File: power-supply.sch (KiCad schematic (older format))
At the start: 0 parts

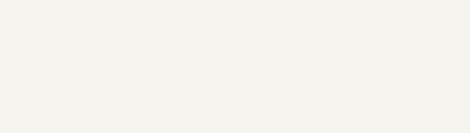
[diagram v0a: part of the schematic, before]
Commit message: Changed the controller symbol for the LPC11C24 added some of the support components,played with the larger blocks
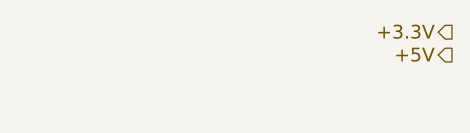
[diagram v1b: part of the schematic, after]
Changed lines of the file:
@@
-EESchema Schematic File Version 2  date 4/14/2013 3:01:00 AM
+EESchema Schematic File Version 2  date 4/14/2013 3:47:51 AM
 LIBS:power
 LIBS:device
@@
 $Descr A4 11693 8268
 encoding utf-8
-Sheet 4 6
+Sheet 6 6
 Title ""
 Date "14 apr 2013"
@@
 Text HLabel 2350 3400 0    60   UnSpc ~ 0
 GND
+Text HLabel 8950 3100 0    60   Output ~ 0
++3.3V
+Text HLabel 8950 3200 0    60   Output ~ 0
++5V
 $EndSCHEMATC

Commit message: changed the voltage lbaels to global labels
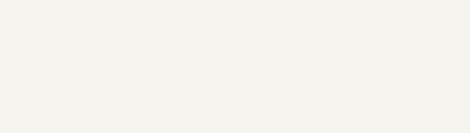
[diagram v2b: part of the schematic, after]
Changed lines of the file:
@@
-EESchema Schematic File Version 2  date 4/14/2013 3:47:51 AM
+EESchema Schematic File Version 2  date 4/14/2013 1:14:12 PM
 LIBS:power
 LIBS:device
@@
 $Descr A4 11693 8268
 encoding utf-8
-Sheet 6 6
+Sheet 6 7
 Title ""
 Date "14 apr 2013"
@@
 Text HLabel 2350 3400 0    60   UnSpc ~ 0
 GND
-Text HLabel 8950 3100 0    60   Output ~ 0
-+3.3V
-Text HLabel 8950 3200 0    60   Output ~ 0
-+5V
 $EndSCHEMATC

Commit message: did the power sheet
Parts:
- added C?: 10uF, ~, symbol C
- added C? (x2): 100nF, ~, symbol C
- added C?: 3.3nF, ~, symbol C
- added C?: C, ~, symbol C
- added C?: 22uF, ~, symbol C
- added C?: 22nF, ~, symbol C
- added L?: 15uH, ~, symbol INDUCTOR
- added R?: 62k, ~, symbol R
- added R?: 11.8k, ~, symbol R
- added R?: 20k, ~, symbol R
- added R?: 20, ~, symbol R
- added U?: RT7247AHGSP, symbol RT7247AHGSP
- added U?: LM137H, TO-39, symbol LM137H
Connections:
- net labels added: +3.3V, +5V
- wire segments 0 -> 41

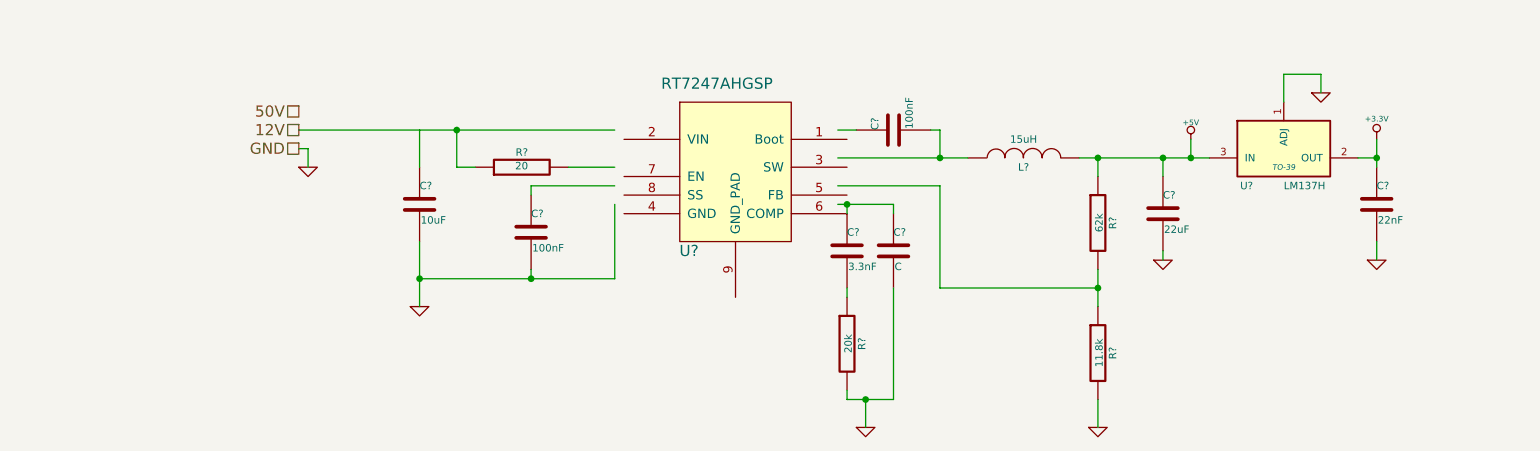
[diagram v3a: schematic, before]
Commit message: updated the power circut to include the more hidden preferences on the data sheet
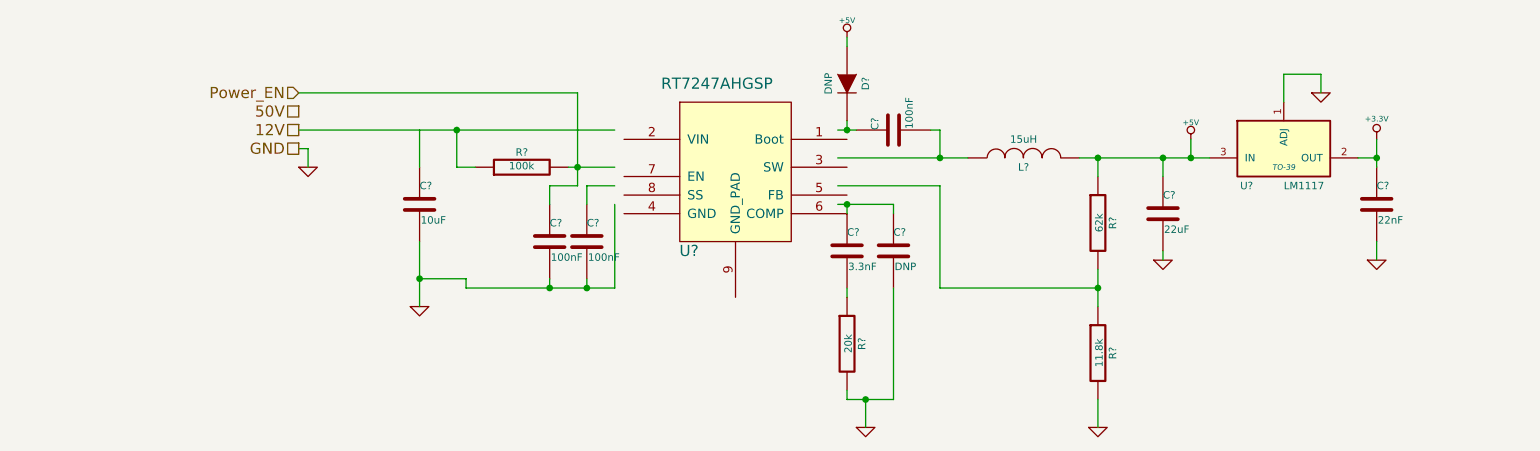
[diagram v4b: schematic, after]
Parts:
- added C?: 100nF, ~, symbol C
- added D?: DNP, ~, symbol DIODE
- C?: value C -> DNP
- R?: value 20 -> 100k
- U?: value LM137H -> LM1117
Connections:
- net labels added: Power_EN
- wire segments 41 -> 65
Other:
- moved on the sheet: C?
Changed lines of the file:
@@
-EESchema Schematic File Version 2  date 4/15/2013 12:24:14 AM
+EESchema Schematic File Version 2  date 4/15/2013 12:46:04 AM
 LIBS:power
 LIBS:device
@@
 L C C?
 U 1 1 516B7AF4
-P 3600 3700
-F 0 "C?" H 3600 3800 40  0000 L CNN
-F 1 "100nF" H 3606 3615 40  0000 L CNN
-F 2 "~" H 3638 3550 30  0000 C CNN
-F 3 "~" H 3600 3700 60  0000 C CNN
-	1    3600 3700
+P 3900 3750
+F 0 "C?" H 3900 3850 40  0000 L CNN
+F 1 "100nF" H 3906 3665 40  0000 L CNN
+F 2 "~" H 3938 3600 30  0000 C CNN
+F 3 "~" H 3900 3750 60  0000 C CNN
+	1    3900 3750
 	1    0    0    -1
 $EndComp
@@
 P 5550 3800
 F 0 "C?" H 5550 3900 40  0000 L CNN
-F 1 "C" H 5556 3715 40  0000 L CNN
+F 1 "DNP" H 5556 3715 40  0000 L CNN
 F 2 "~" H 5588 3650 30  0000 C CNN
 F 3 "~" H 5550 3800 60  0000 C CNN
@@
 $EndComp
 Wire Wire Line
-	2350 3150 4050 3150
-Wire Wire Line
-	3000 3750 3000 4100
+	2350 3150 3200 3150
+Wire Wire Line
+	3200 3150 4050 3150
+Wire Wire Line
+	3000 3750 3000 3950
+Wire Wire Line
+	3000 3950 3000 4100
 Wire Wire Line
 	3000 3350 3000 3150
 Wire Wire Line
-	3600 3500 3600 3450
-Wire Wire Line
-	3600 3450 4050 3450
-Wire Wire Line
-	4050 3950 4050 3550
-Wire Wire Line
-	3000 3950 4050 3950
-Wire Wire Line
-	3600 3950 3600 3900
+	3900 3550 3900 3450
+Wire Wire Line
+	3900 3450 4050 3450
+Wire Wire Line
+	4050 4000 4050 3550
+Wire Wire Line
+	3000 3950 3250 3950
+Wire Wire Line
+	3250 4000 3700 4000
+Wire Wire Line
+	3700 4000 3900 4000
+Wire Wire Line
+	3900 4000 4050 4000
+Wire Wire Line
+	3900 4000 3900 3950
 Connection ~ 3000 3950
-Connection ~ 3600 3950
 Wire Wire Line
 	5300 3600 5300 3550
 Wire Wire Line
-	5250 3550 5550 3550
+	5250 3550 5300 3550
+Wire Wire Line
+	5300 3550 5550 3550
 Wire Wire Line
 	5550 3550 5550 3600
@@
 	5550 4600 5550 4000
 Wire Wire Line
-	5300 4600 5550 4600
+	5300 4600 5400 4600
+Wire Wire Line
+	5400 4600 5550 4600
 Wire Wire Line
 	5300 4600 5300 4550
@@
 	5300 4050 5300 4000
 Wire Wire Line
-	5250 3300 5950 3300
+	5250 3300 5800 3300
+Wire Wire Line
+	5800 3300 5950 3300
 Wire Wire Line
 	5250 3450 5800 3450
@@
 	5800 4000 6650 4000
 Wire Wire Line
-	6650 3900 6650 4100
+	6650 3900 6650 4000
+Wire Wire Line
+	6650 4000 6650 4100
 Connection ~ 6650 4000
 Wire Wire Line
 	6650 3400 6650 3300
 Wire Wire Line
-	6550 3300 7250 3300
+	6550 3300 6650 3300
+Wire Wire Line
+	6650 3300 7000 3300
+Wire Wire Line
+	7000 3300 7150 3300
+Wire Wire Line
+	7150 3300 7250 3300
 Wire Wire Line
 	5800 3450 5800 4000
 Wire Wire Line
-	5250 3150 5350 3150
+	5250 3150 5300 3150
+Wire Wire Line
+	5300 3150 5350 3150
 Wire Wire Line
 	5800 3150 5750 3150
@@
 P 7650 3250
 F 0 "U?" H 7450 3050 40  0000 C CNN
-F 1 "LM137H" H 7650 3050 40  0000 L CNN
+F 1 "LM1117" H 7650 3050 40  0000 L CNN
 F 2 "TO-39" H 7650 3150 30  0000 C CIN
 F 3 "~" H 7650 3250 60  0000 C CNN
@@
 	8050 3300 8150 3300
 Wire Wire Line
-	8150 3200 8150 3350
+	8150 3200 8150 3300
+Wire Wire Line
+	8150 3300 8150 3350
 $Comp
 L C C?
@@
 P 3550 3350
 F 0 "R?" V 3630 3350 40  0000 C CNN
-F 1 "20" V 3557 3351 40  0000 C CNN
+F 1 "100k" V 3557 3351 40  0000 C CNN
 F 2 "~" V 3480 3350 30  0000 C CNN
 F 3 "~" H 3550 3350 30  0000 C CNN
@@
 Connection ~ 3200 3150
 Wire Wire Line
-	3800 3350 4050 3350
+	3800 3350 3850 3350
+Wire Wire Line
+	3850 3350 4050 3350
 $Comp
 L GND #PWR?
@@
 Wire Wire Line
 	2400 3250 2350 3250
+$Comp
+L DIODE D?
+U 1 1 516B8761
+P 5300 2900
+F 0 "D?" H 5300 3000 40  0000 C CNN
+F 1 "DNP" H 5300 2800 40  0000 C CNN
+F 2 "~" H 5300 2900 60  0000 C CNN
+F 3 "~" H 5300 2900 60  0000 C CNN
+	1    5300 2900
+	0    1    1    0
+$EndComp
+Wire Wire Line
+	5300 3100 5300 3150
+Connection ~ 5300 3150
+$Comp
+L +5V #PWR?
+U 1 1 516B87A2
+P 5300 2650
+F 0 "#PWR?" H 5300 2740 20  0001 C CNN
+F 1 "+5V" H 5300 2740 30  0000 C CNN
+F 2 "" H 5300 2650 60  0000 C CNN
+F 3 "" H 5300 2650 60  0000 C CNN
+	1    5300 2650
+	1    0    0    -1
+$EndComp
+Wire Wire Line
+	5300 2700 5300 2650
+$Comp
+L C C?
+U 1 1 516B8BF3
+P 3700 3750
+F 0 "C?" H 3700 3850 40  0000 L CNN
+F 1 "100nF" H 3706 3665 40  0000 L CNN
+F 2 "~" H 3738 3600 30  0000 C CNN
+F 3 "~" H 3700 3750 60  0000 C CNN
+	1    3700 3750
+	1    0    0    -1
+$EndComp
+Wire Wire Line
+	3250 3950 3250 4000
+Connection ~ 3900 4000
+Wire Wire Line
+	3700 3950 3700 4000
+Connection ~ 3700 4000
+Wire Wire Line
+	3700 3550 3700 3450
+Wire Wire Line
+	3850 3450 3700 3450
+Wire Wire Line
+	3850 2950 3850 3350
+Wire Wire Line
+	3850 3350 3850 3450
+Connection ~ 3850 3350
+Text HLabel 2350 2950 0    60   Input ~ 0
+Power_EN
+Wire Wire Line
+	2350 2950 3850 2950
 $EndSCHEMATC

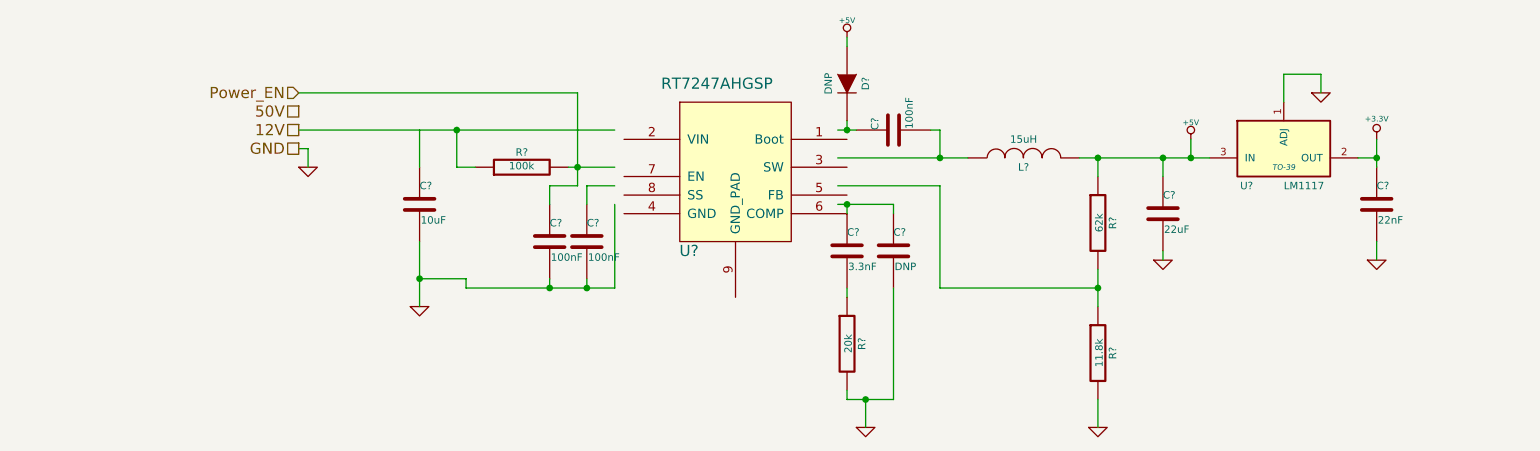
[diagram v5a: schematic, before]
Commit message: power updated still need to add underpad also changed input connector to 5 pin and added fuses, added current sense with op-amp for solinoids
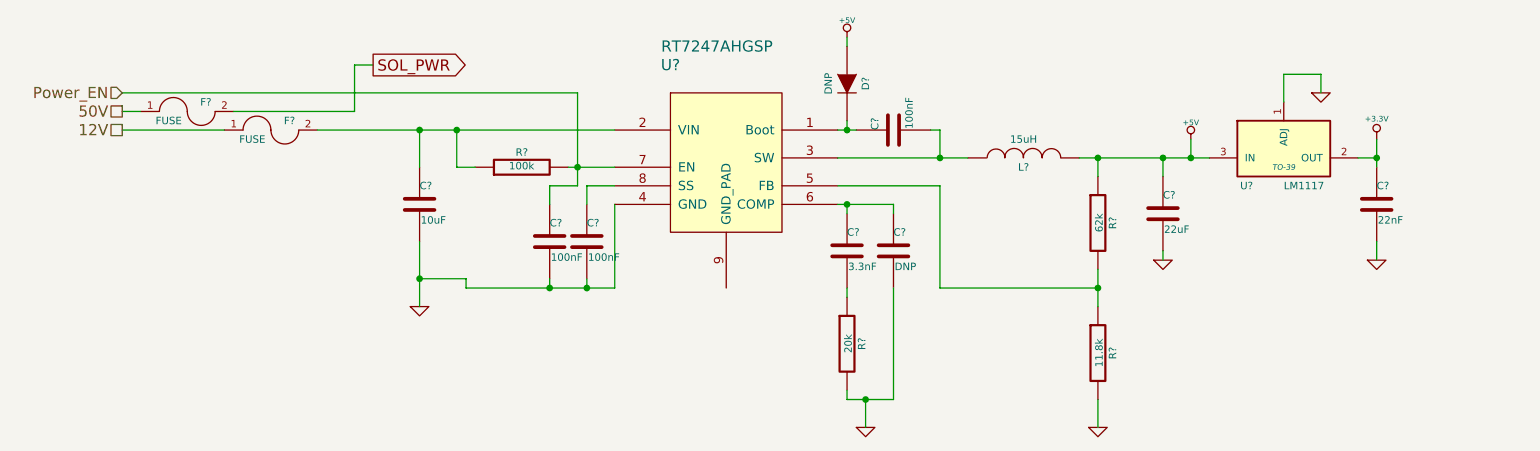
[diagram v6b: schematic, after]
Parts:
- removed U?: RT7247AHGSP, symbol RT7247AHGSP
- added F? (x2): FUSE, ~, symbol FUSE
- added U?: RT7247AHGSP, symbol RT7247AHGSP
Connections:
- net labels added: SOL_PWR
- wire segments 65 -> 53
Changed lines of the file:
@@
-EESchema Schematic File Version 2  date 4/15/2013 1:22:57 AM
+EESchema Schematic File Version 2  date 4/16/2013 12:48:50 AM
 LIBS:power
 LIBS:device
@@
 LIBS:pinball_components
 LIBS:micro-controller
+LIBS:CurrentSense
+LIBS:pinball-power
 LIBS:base-module-cache
 EELAYER 27 0
@@
 $Descr A4 11693 8268
 encoding utf-8
-Sheet 7 7
+Sheet 6 8
 Title ""
-Date "15 apr 2013"
+Date "16 apr 2013"
 Rev ""
 Comp ""
@@
 Comment4 ""
 $EndDescr
-Text HLabel 2350 3050 0    60   UnSpc ~ 0
+Text HLabel 1400 3050 0    60   UnSpc ~ 0
 50V
-Text HLabel 2350 3150 0    60   UnSpc ~ 0
+Text HLabel 1400 3150 0    60   UnSpc ~ 0
 12V
-Text HLabel 2350 3250 0    60   UnSpc ~ 0
-GND
-$Comp
-L RT7247AHGSP U?
-U 1 1 516B7ABB
-P 4650 3400
-F 0 "U?" H 4450 3000 60  0000 C CNN
-F 1 "RT7247AHGSP" H 4600 3900 60  0000 C CNN
-F 2 "" H 4650 3400 60  0000 C CNN
-F 3 "" H 4650 3400 60  0000 C CNN
-	1    4650 3400
-	1    0    0    -1
-$EndComp
 $Comp
 L C C?
@@
 	1    0    0    -1
 $EndComp
-Wire Wire Line
-	2350 3150 3200 3150
-Wire Wire Line
-	3200 3150 4050 3150
-Wire Wire Line
-	3000 3750 3000 3950
-Wire Wire Line
-	3000 3950 3000 4100
-Wire Wire Line
-	3000 3350 3000 3150
-Wire Wire Line
-	3900 3550 3900 3450
-Wire Wire Line
-	3900 3450 4050 3450
-Wire Wire Line
-	4050 4000 4050 3550
-Wire Wire Line
-	3000 3950 3250 3950
-Wire Wire Line
-	3250 4000 3700 4000
-Wire Wire Line
-	3700 4000 3900 4000
-Wire Wire Line
-	3900 4000 4050 4000
-Wire Wire Line
-	3900 4000 3900 3950
-Connection ~ 3000 3950
-Wire Wire Line
-	5300 3600 5300 3550
-Wire Wire Line
-	5250 3550 5300 3550
-Wire Wire Line
-	5300 3550 5550 3550
-Wire Wire Line
-	5550 3550 5550 3600
-Connection ~ 5300 3550
-Wire Wire Line
-	5550 4600 5550 4000
-Wire Wire Line
-	5300 4600 5400 4600
-Wire Wire Line
-	5400 4600 5550 4600
-Wire Wire Line
-	5300 4600 5300 4550
-Wire Wire Line
-	5300 4050 5300 4000
-Wire Wire Line
-	5250 3300 5800 3300
-Wire Wire Line
-	5800 3300 5950 3300
-Wire Wire Line
-	5250 3450 5800 3450
-Wire Wire Line
-	5800 4000 6650 4000
-Wire Wire Line
-	6650 3900 6650 4000
-Wire Wire Line
-	6650 4000 6650 4100
-Connection ~ 6650 4000
-Wire Wire Line
-	6650 3400 6650 3300
-Wire Wire Line
-	6550 3300 6650 3300
-Wire Wire Line
-	6650 3300 7000 3300
-Wire Wire Line
-	7000 3300 7150 3300
-Wire Wire Line
-	7150 3300 7250 3300
-Wire Wire Line
-	5800 3450 5800 4000
-Wire Wire Line
-	5250 3150 5300 3150
-Wire Wire Line
-	5300 3150 5350 3150
-Wire Wire Line
-	5800 3150 5750 3150
-Wire Wire Line
-	5800 3300 5800 3150
-Connection ~ 5800 3300
-Wire Wire Line
-	6650 4750 6650 4600
-Wire Wire Line
-	5400 4750 5400 4600
-Connection ~ 5400 4600
-Connection ~ 6650 3300
 $Comp
 L GND #PWR?
@@
 	1    0    0    -1
 $EndComp
-Wire Wire Line
-	7000 3850 7000 3800
 $Comp
 L +5V #PWR?
@@
 	1    0    0    -1
 $EndComp
-Wire Wire Line
-	7150 3300 7150 3200
-Wire Wire Line
-	7000 3400 7000 3300
-Connection ~ 7000 3300
 $Comp
 L LM137H U?
@@
 	1    0    0    -1
 $EndComp
-Connection ~ 7150 3300
 $Comp
 L GND #PWR?
@@
 	1    0    0    -1
 $EndComp
-Wire Wire Line
-	7850 2950 7850 2850
-Wire Wire Line
-	7850 2850 7650 2850
-Wire Wire Line
-	7650 2850 7650 3000
 $Comp
 L +3.3V #PWR?
@@
 	1    0    0    -1
 $EndComp
-Wire Wire Line
-	8050 3300 8150 3300
-Wire Wire Line
-	8150 3200 8150 3300
-Wire Wire Line
-	8150 3300 8150 3350
 $Comp
 L C C?
@@
 	1    0    0    -1
 $EndComp
-Wire Wire Line
-	8150 3850 8150 3750
-Connection ~ 8150 3300
 $Comp
 L R R?
@@
 	0    -1   -1   0
 $EndComp
-Wire Wire Line
-	3300 3350 3200 3350
-Wire Wire Line
-	3200 3350 3200 3150
-Connection ~ 3200 3150
-Wire Wire Line
-	3800 3350 3850 3350
-Wire Wire Line
-	3850 3350 4050 3350
-$Comp
-L GND #PWR?
-U 1 1 516B82F2
-P 2400 3350
-F 0 "#PWR?" H 2400 3350 30  0001 C CNN
-F 1 "GND" H 2400 3280 30  0001 C CNN
-F 2 "" H 2400 3350 60  0000 C CNN
-F 3 "" H 2400 3350 60  0000 C CNN
-	1    2400 3350
-	1    0    0    -1
-$EndComp
-Wire Wire Line
-	2400 3350 2400 3250
-Wire Wire Line
-	2400 3250 2350 3250
 $Comp
 L DIODE D?
@@
 	0    1    1    0
 $EndComp
-Wire Wire Line
-	5300 3100 5300 3150
-Connection ~ 5300 3150
 $Comp
 L +5V #PWR?
@@
 	1    0    0    -1
 $EndComp
-Wire Wire Line
-	5300 2700 5300 2650
 $Comp
 L C C?
@@
 	1    0    0    -1
 $EndComp
+Text HLabel 1400 2950 0    60   Input ~ 0
+Power_EN
+Wire Wire Line
+	3000 3750 3000 4100
+Wire Wire Line
+	3000 3350 3000 3150
+Wire Wire Line
+	3900 3550 3900 3450
+Wire Wire Line
+	3900 3450 4050 3450
+Wire Wire Line
+	4050 4000 4050 3550
+Wire Wire Line
+	3000 3950 3250 3950
+Wire Wire Line
+	3250 4000 4050 4000
+Wire Wire Line
+	3900 4000 3900 3950
+Connection ~ 3000 3950
+Wire Wire Line
+	5300 3600 5300 3550
+Wire Wire Line
+	5250 3550 5550 3550
+Wire Wire Line
+	5550 3550 5550 3600
+Connection ~ 5300 3550
+Wire Wire Line
+	5550 4600 5550 4000
+Wire Wire Line
+	5300 4600 5550 4600
+Wire Wire Line
+	5300 4600 5300 4550
+Wire Wire Line
+	5300 4050 5300 4000
+Wire Wire Line
+	5250 3300 5950 3300
+Wire Wire Line
+	5250 3450 5800 3450
+Wire Wire Line
+	5800 4000 6650 4000
+Wire Wire Line
+	6650 3900 6650 4100
+Connection ~ 6650 4000
+Wire Wire Line
+	6650 3400 6650 3300
+Wire Wire Line
+	6550 3300 7250 3300
+Wire Wire Line
+	5800 3450 5800 4000
+Wire Wire Line
+	5250 3150 5350 3150
+Wire Wire Line
+	5800 3150 5750 3150
+Wire Wire Line
+	5800 3300 5800 3150
+Connection ~ 5800 3300
+Wire Wire Line
+	6650 4750 6650 4600
+Wire Wire Line
+	5400 4750 5400 4600
+Connection ~ 5400 4600
+Connection ~ 6650 3300
+Wire Wire Line
+	7000 3850 7000 3800
+Wire Wire Line
+	7150 3300 7150 3200
+Wire Wire Line
+	7000 3400 7000 3300
+Connection ~ 7000 3300
+Connection ~ 7150 3300
+Wire Wire Line
+	7850 2950 7850 2850
+Wire Wire Line
+	7850 2850 7650 2850
+Wire Wire Line
+	7650 2850 7650 3000
+Wire Wire Line
+	8050 3300 8150 3300
+Wire Wire Line
+	8150 3200 8150 3350
+Wire Wire Line
+	8150 3850 8150 3750
+Connection ~ 8150 3300
+Wire Wire Line
+	3300 3350 3200 3350
+Wire Wire Line
+	3200 3350 3200 3150
+Connection ~ 3200 3150
+Wire Wire Line
+	3800 3350 4050 3350
+Wire Wire Line
+	5300 3100 5300 3150
+Connection ~ 5300 3150
+Wire Wire Line
+	5300 2700 5300 2650
 Wire Wire Line
 	3250 3950 3250 4000
@@
 	3700 3550 3700 3450
 Wire Wire Line
-	3850 3450 3700 3450
-Wire Wire Line
-	3850 2950 3850 3350
-Wire Wire Line
-	3850 3350 3850 3450
+	3700 3450 3850 3450
+Wire Wire Line
+	3850 3450 3850 2950
 Connection ~ 3850 3350
-Text HLabel 2350 2950 0    60   Input ~ 0
-Power_EN
-Wire Wire Line
-	2350 2950 3850 2950
+Wire Wire Line
+	3850 2950 1400 2950
+Connection ~ 3000 3150
+Wire Wire Line
+	2650 3050 2650 2800
+Text GLabel 2750 2800 2    60   Output ~ 0
+SOL_PWR
+Wire Wire Line
+	2650 2800 2750 2800
+$Comp
+L FUSE F?
+U 1 1 516D27EC
+P 1750 3050
+F 0 "F?" H 1850 3100 40  0000 C CNN
+F 1 "FUSE" H 1650 3000 40  0000 C CNN
+F 2 "~" H 1750 3050 60  0000 C CNN
+F 3 "~" H 1750 3050 60  0000 C CNN
+	1    1750 3050
+	1    0    0    -1
+$EndComp
+Wire Wire Line
+	4050 3150 2450 3150
+$Comp
+L FUSE F?
+U 1 1 516D2839
+P 2200 3150
+F 0 "F?" H 2300 3200 40  0000 C CNN
+F 1 "FUSE" H 2100 3100 40  0000 C CNN
+F 2 "~" H 2200 3150 60  0000 C CNN
+F 3 "~" H 2200 3150 60  0000 C CNN
+	1    2200 3150
+	1    0    0    -1
+$EndComp
+Wire Wire Line
+	1950 3150 1400 3150
+Wire Wire Line
+	1500 3050 1400 3050
+Wire Wire Line
+	2000 3050 2650 3050
+$Comp
+L RT7247AHGSP U?
+U 1 1 516D349F
+P 4600 3350
+F 0 "U?" H 4350 3900 60  0000 C CNN
+F 1 "RT7247AHGSP" H 4600 4000 60  0000 C CNN
+F 2 "" H 4600 3350 60  0000 C CNN
+F 3 "" H 4600 3350 60  0000 C CNN
+	1    4600 3350
+	1    0    0    -1
+$EndComp
 $EndSCHEMATC
